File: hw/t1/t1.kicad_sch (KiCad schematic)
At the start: 65 parts, among them J1 SFP edge (INF-8074i), J2 Rosenberger E6S20A-40MT5-Z (H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, U1 DP83TG720S-Q1 (or DP83TC812S-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, U2 STM32G031F6P6, U3 TPS62822DLC, U4 TPS22918DBVR, Y1 25MHz CL8pF 2016

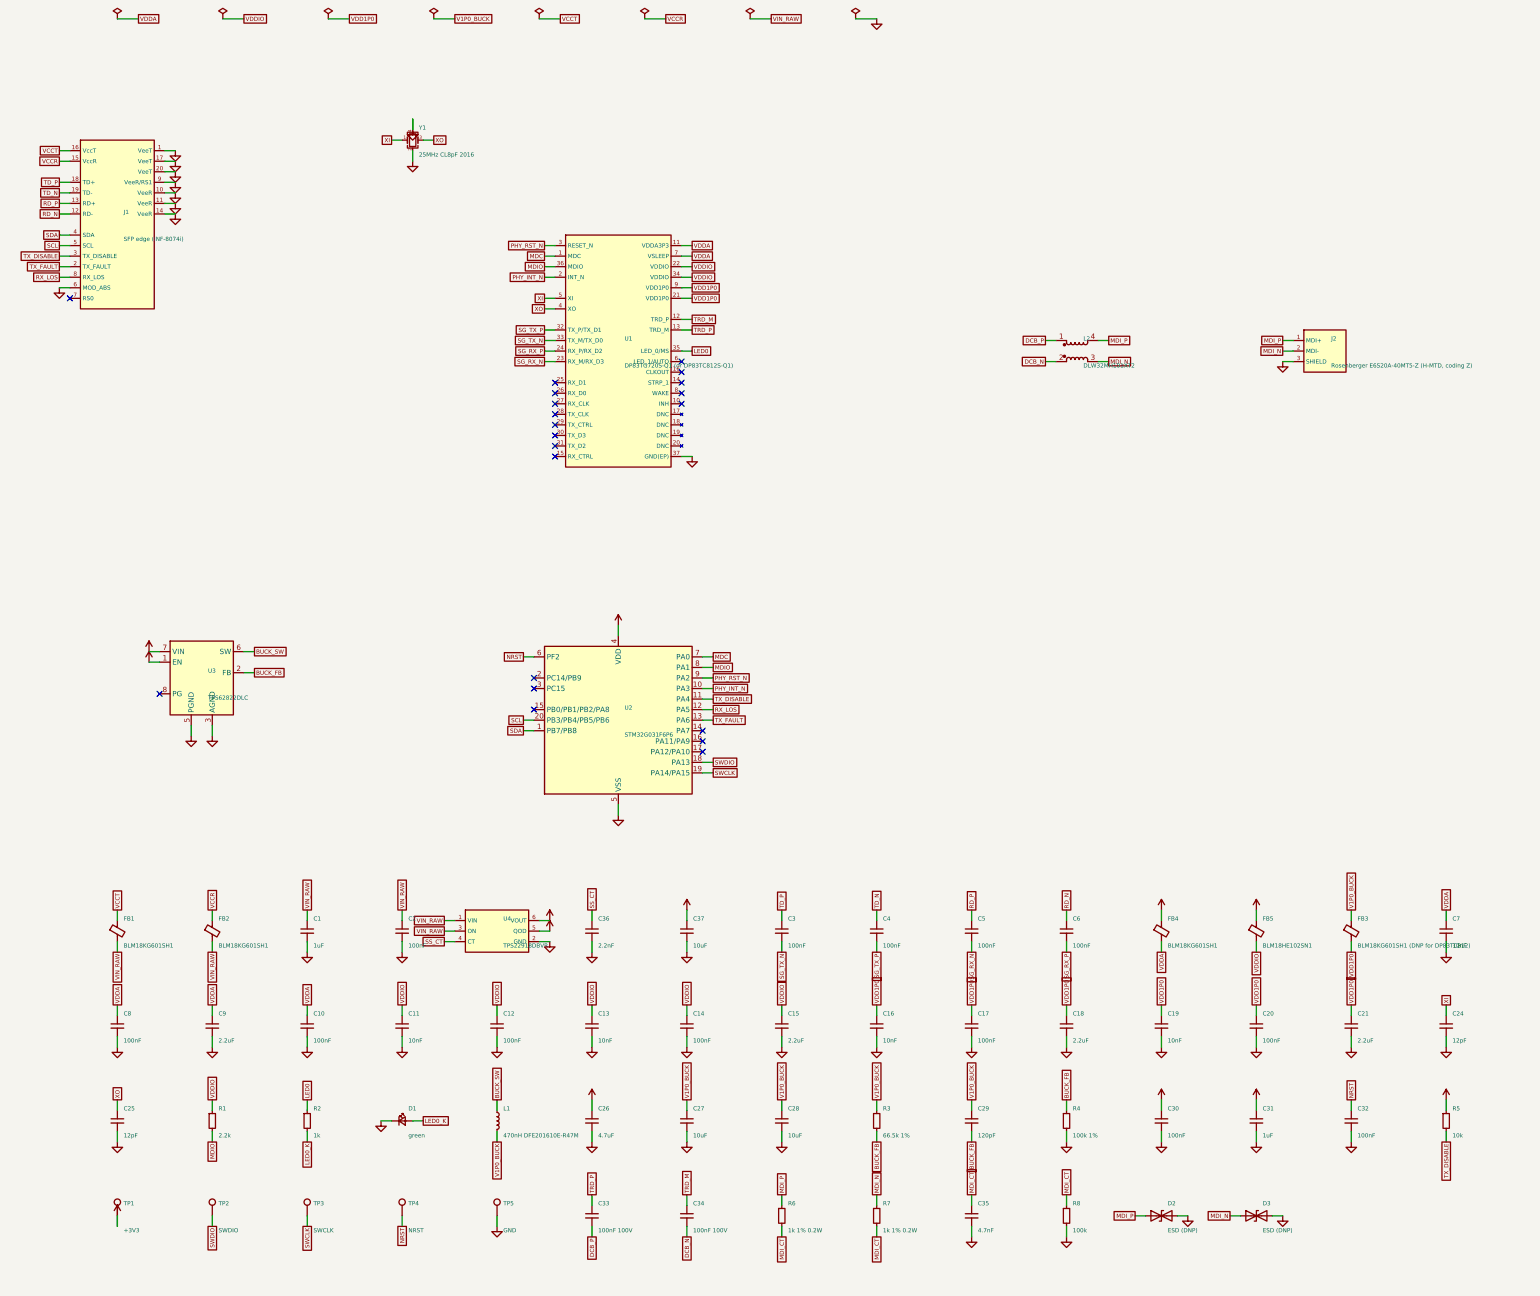
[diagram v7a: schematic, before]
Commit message: SFP edge was mirrored: fix the pad order, re-lay T1
The edge footprint put pin 20 at the top seen from above with the card edge
on the left; SFF-8419 Figure 7-2 (and INF-8074i Figure 2, drawn the other
way round) has pin 11 there. Every host contact would have landed between
two pads, VccT against ground. pad_y() is negated, the ground-finger vias
follow, and tools/compliance.py now states the expected positions itself.

T1, re-laid on the corrected edge:
- TD reaches the PHY's TX pins and RD its RX pins straight, P to P, both on
  top; the SGMII polarity-invert bits the firmware used to set are gone
- DP83TG720 EP 3.7 mm (RHA0036A), not 4.1
- XI series resistor R9: 0 ohm for the DP83TG720, 100 ohm in the DP83TC812
  loadout (SNLS654D Table 5-1)
- firmware clears SGMII AN on the DP83TC812 (SNLS654D 7.4.12.4)

Shared footprints: CMC land to TDK ACT1210E / Murata DLW32MH (1.05 x 0.6
pads, 0.4 between lines, 2.0 inner gap), H-MTD front solder area 2.2 wide
(MB_633), board thickness 1.0 mm in the files.

RJ45 and T1S still carry the mirrored edge; the README says not to order.
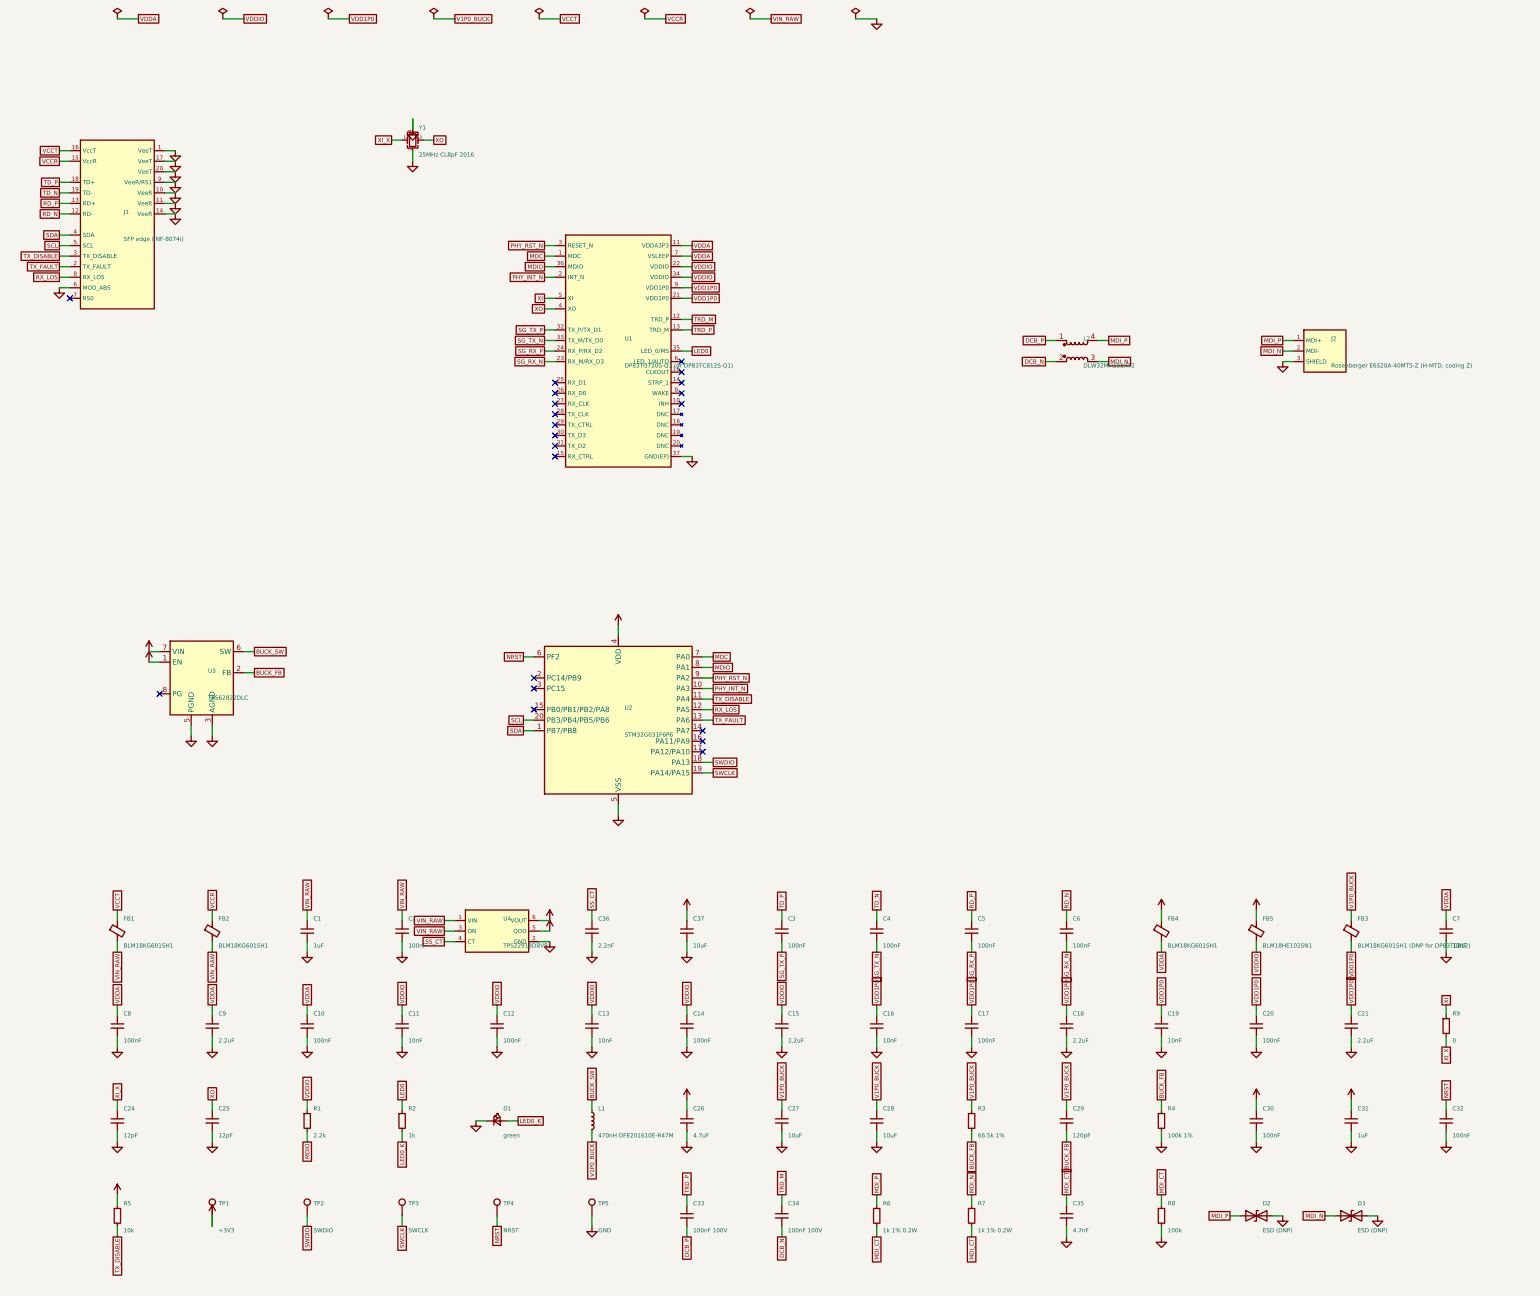
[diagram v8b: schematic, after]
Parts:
- added R9: 0, Resistor_SMD:R_0201_0603Metric, symbol Device:R_Small
- U1: footprint Package_DFN_QFN:QFN-36-1EP_6x6mm_P0.5mm_EP4.1x4.1mm_ThermalVias -> Package_DFN_QFN:QFN-36-1EP_6x6mm_P0.5mm_EP3.7x3.7mm_ThermalVias
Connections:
- net SG_RX_N: now also C6.2; no longer C5.2
- net SG_RX_P: now also C5.2; no longer C6.2
- net SG_TX_N: now also C4.2; no longer C3.2
- net SG_TX_P: now also C3.2; no longer C4.2
- net XI: now also R9.1; no longer C24.1, Y1.1
- new net XI_X: C24.1, R9.2, Y1.1
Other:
- moved on the sheet: C24, C25, C26, C27, C28, C29, C30, C31, C32, C33, C34, C35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
